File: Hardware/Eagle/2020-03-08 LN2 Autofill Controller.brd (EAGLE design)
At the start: 114.3 x 95.2 mm, 28 parts, among them SW1 Omron B3J-2100, SW2 Omron B3J-2100, SW3 Omron B3J-2100, SW4 Omron B3J-2100, U1 MC14490DWG, U3 ISO7421DR

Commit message: Removed bottom polygon (missed some before)
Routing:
- removed copper zone on layer 16, net +5V
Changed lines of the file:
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@@
 <wire x1="93.472" y1="38.227" x2="93.98" y2="38.735" width="0.4064" layer="1"/>
 <wire x1="93.98" y1="38.735" x2="93.98" y2="45.085" width="0.4064" layer="1"/>
-<polygon width="0.254" layer="16">
-<vertex x="114.3" y="0"/>
-<vertex x="114.3" y="66.04"/>
-<vertex x="113.03" y="67.31"/>
-<vertex x="106.68" y="67.31"/>
-<vertex x="102.87" y="71.12"/>
-<vertex x="102.87" y="76.2"/>
-<vertex x="106.68" y="80.01"/>
-<vertex x="113.03" y="80.01"/>
-<vertex x="114.3" y="81.28"/>
-<vertex x="114.3" y="95.25"/>
-</polygon>
 <wire x1="54.93" y1="59.69" x2="53.34" y2="59.69" width="0.4064" layer="1"/>
 <wire x1="52.3808" y1="60.6492" x2="52.3808" y2="62.865" width="0.4064" layer="1"/>
@@
 <via x="47.625" y="62.865" extent="1-16" drill="0.35"/>
 <contactref element="LCD1" pad="3"/>
+<wire x1="52.3808" y1="62.865" x2="50.8" y2="88.9" width="0" layer="19" extent="1-1"/>
+<wire x1="33.655" y1="64.45" x2="47.625" y2="62.865" width="0" layer="19" extent="16-16"/>
+<wire x1="29.845" y1="64.45" x2="33.655" y2="64.45" width="0" layer="19" extent="16-16"/>
+<wire x1="25.4" y1="58.42" x2="29.845" y2="64.45" width="0" layer="19" extent="16-16"/>
+<wire x1="66.04" y1="48.895" x2="54.93" y2="59.69" width="0" layer="19" extent="1-1"/>
+<wire x1="92.0375" y1="38.227" x2="66.04" y2="48.895" width="0" layer="19" extent="1-1"/>
 <wire x1="93.98" y1="11.43" x2="92.395" y2="35.56" width="0" layer="19" extent="1-1"/>
+<wire x1="14.29" y1="20.955" x2="25.4" y2="58.42" width="0" layer="19" extent="1-1"/>
 </signal>
 <signal name="THER4-SIG">

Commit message: Start rewiring
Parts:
- removed TP1: (no value), AUmlib:TESTPOINT1
- added TP3: TP5000-TESTPOINT-BLK, AUmlib:TP5000-TESTPOINT-BLK
- TP2: value (none) -> TP5000-TESTPOINT-BLU; device AUmlib:TESTPOINT1 -> AUmlib:TP5000-TESTPOINT-BLU
- moved R5 21.6 mm to (34.9, 31.8), flipped to the top
- moved TP2 12.7 mm to (19.1, 12.1)
- moved C1 2.29 mm to (97.8, 48.9)
- moved C2 1.90 mm to (13.3, 21.0), turned to 180 degrees
- moved R4 0.71 mm to (30.5, 63.2), flipped to the top
- moved R3 0.71 mm to (33.0, 63.2), flipped to the top
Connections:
- net A1IN: no longer TP1.1
- net GND: now also TP3.P$1; no longer TP2.1
- net PRES: now also TP2.P$1
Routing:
- net A1IN: track 69.7 -> 0.00 mm, vias 1 -> 0
- net +5V: track 29.3 -> 85.7 mm, vias 3 -> 2
- net N$4: track 4.13 -> 26.0 mm
- net OLED/RES: track 66.9 -> 45.9 mm, vias 1 -> 0
- net LED1-K: track 23.3 -> 28.7 mm
- net +24V: track 11.4 -> 13.9 mm
- net LED1-A: track 33.4 -> 35.7 mm
- net PRES: track 69.2 -> 70.5 mm, vias 1 -> 0
- net GND: track 6.62 -> 5.67 mm
- net SDA: track 97.6 -> 97.0 mm, vias 1 -> 2
- net SCL: track 95.1 -> 94.5 mm, vias 1 -> 0
- added copper zone on layer 16, net GND
- removed copper zone on layer 1, net GND
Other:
- board text added: "PRES"
- board text removed: "A1IN"

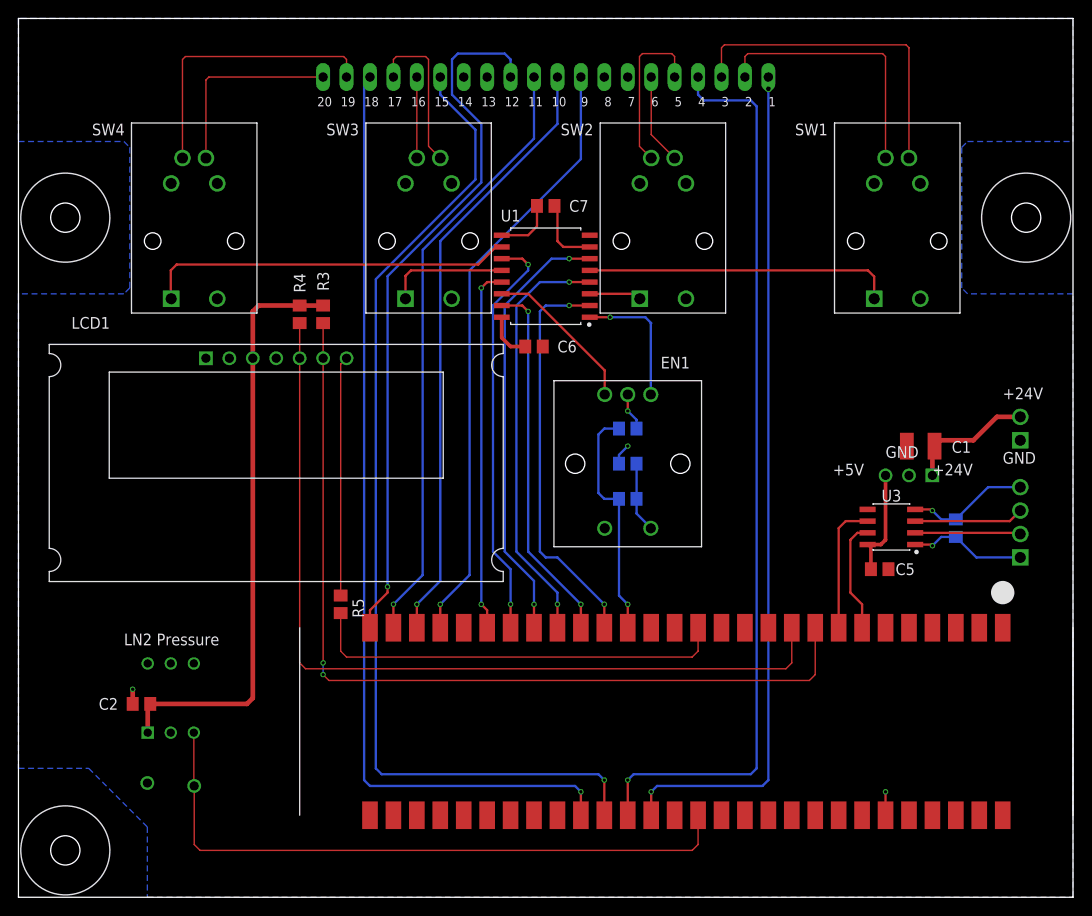
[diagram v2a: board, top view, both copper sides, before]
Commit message: Rerouted controller board, putting most traces on the top
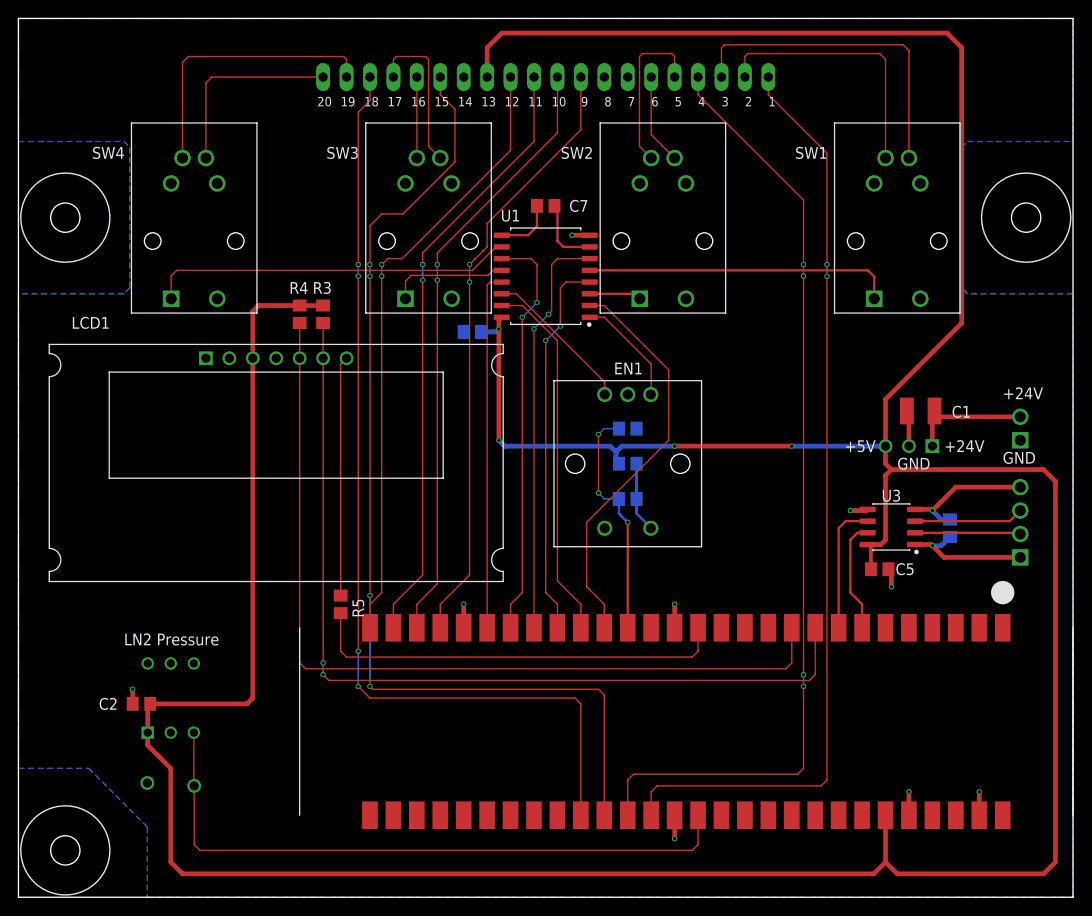
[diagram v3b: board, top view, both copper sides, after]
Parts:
- moved C6 6.85 mm to (49.2, 61.3), flipped to the bottom
- moved C1 3.81 mm to (97.8, 52.7)
- moved PS2 3.18 mm to (96.5, 48.9)
- moved C3 0.63 mm to (101.0, 40.0)
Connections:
- net N$12 renamed VCC1
- net N$15 renamed GND1
- net N$5 renamed AIN
- net N$6 renamed BIN
- removed net VOUT: PS2.3
- net +5V: now also PS2.3
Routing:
- net +5V: track 85.7 -> 419.9 mm, vias 2 -> 4
- net GND: track 5.67 -> 24.1 mm, vias 2 -> 9
- net THER4-SIG: track 76.7 -> 66.9 mm, vias 1 -> 2
- net VALV1: track 92.0 -> 100.9 mm
- net SW3: track 45.8 -> 41.5 mm
- net VALV2: track 98.8 -> 103.1 mm, vias 1 -> 4
- net SW4: track 47.6 -> 44.6 mm
- net AIN: track 14.7 -> 12.1 mm, vias 1 -> 0
- net VCC1: track 12.8 -> 14.3 mm
- net GND1: track 13.3 -> 14.8 mm
- net BIN: track 17.2 -> 16.5 mm
- net SW2: track 39.6 -> 38.9 mm, vias 2 -> 0
- net VALV3: track 110.1 -> 110.7 mm, vias 1 -> 4
- net ENCB: track 43.6 -> 43.9 mm, vias 2 -> 0
- net VALV4: track 103.4 -> 103.6 mm, vias 1 -> 4
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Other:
- board text added: "LED1A"
- board text added: "LED1K"
- board text added: "LED2A"
- board text added: "LED2K"
- board text added: "LED3A"
- board text added: "LED3K"
- board text added: "LED4A"
- board text added: "LED4K"
- board text added: "LN2 Autofill Controller 2020-11-29"
- board text added: "NC"
- board text added: "THER1"
- board text added: "THER2"
- board text added: "THER3"
- board text added: "THER4"
- board text added: "VALV1"
- board text added: "VALV2"
- board text added: "VALV3"
- board text added: "VALV4"
- board text removed: "LN2 Autofill Controller 2020-03-08"

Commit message: Save minor changes?
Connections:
- net N$4 renamed /RES
